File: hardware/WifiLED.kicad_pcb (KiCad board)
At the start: 2 copper layers, 63.5 x 45.7 mm, 22 parts, among them P1 CONN_01X03, P2 CONN_01X03, P3 CONN_01X01, P4 CONN_01X01, P5 CONN_01X01, P6 CONN_01X01

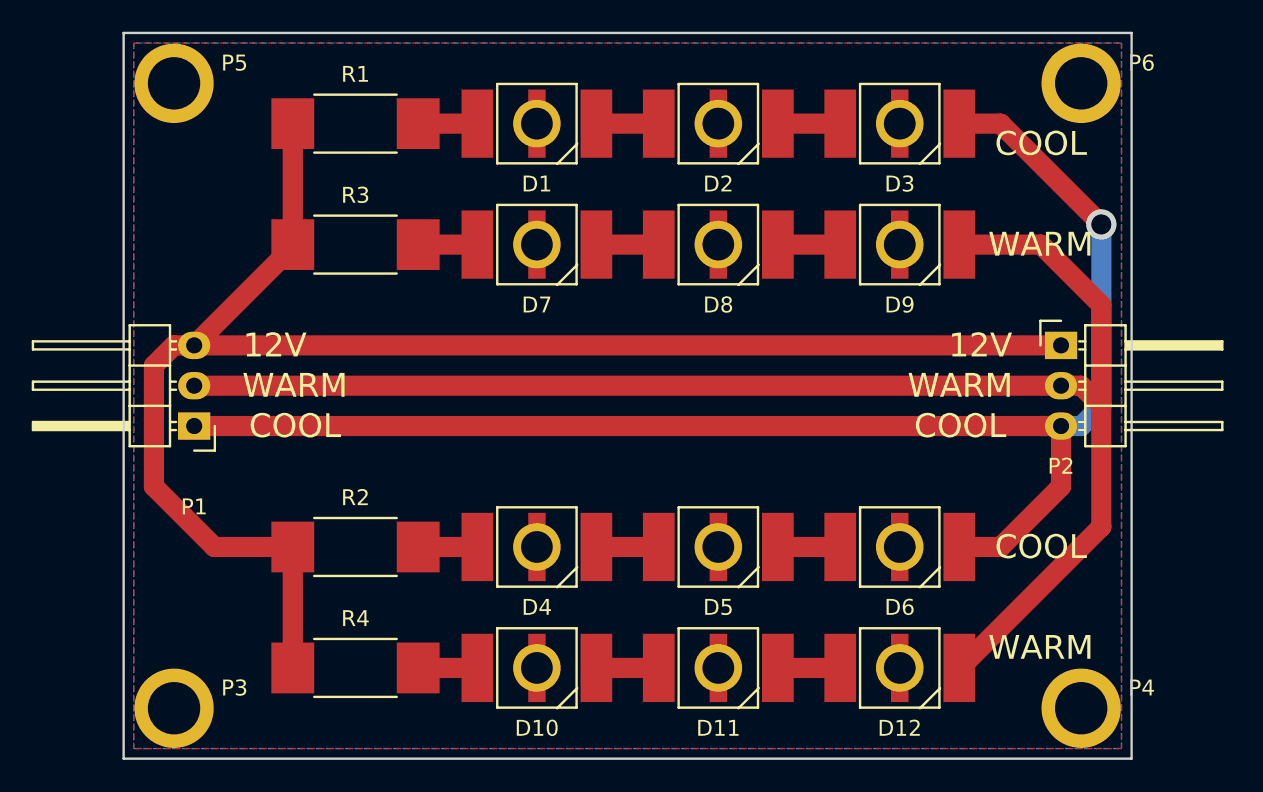
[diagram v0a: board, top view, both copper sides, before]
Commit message: Removed libopencm3 and software
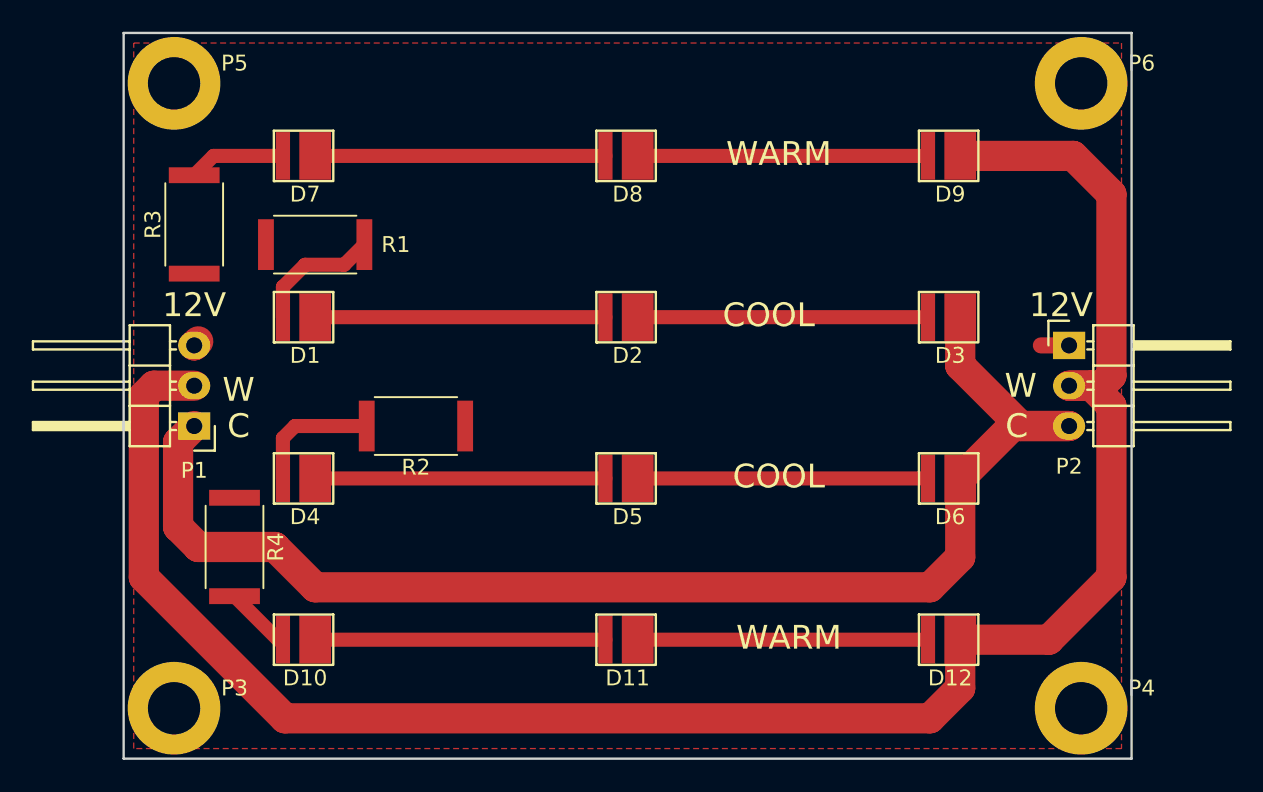
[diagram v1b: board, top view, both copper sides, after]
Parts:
- D1, D10, D11, D12, D2, D3, D4, D5, D6, D7, D8, D9: value LED_tm -> LED; footprint matthew:CREE_MX6 -> matthew:LED3030
- R1, R2, R3, R4: value 6.6R -> 8.2R; footprint Resistors_SMD:R_2512_HandSoldering -> Resistors_SMD:R_2512
- moved D1 18.9 mm to (143.5, 96.5), turned to 180 degrees
- moved D3 14.9 mm to (184.2, 96.5), turned to 180 degrees
- moved D2 14.5 mm to (163.8, 96.5), turned to 180 degrees
- moved D7 13.3 mm to (143.5, 86.4), turned to 180 degrees
- moved D4 13.0 mm to (143.5, 106.7), turned to 180 degrees
- moved D10 12.7 mm to (143.5, 116.8), turned to 180 degrees
- moved R4 10.8 mm to (137.2, 109.2), turned to 270 degrees
- moved R3 10.2 mm to (134.6, 88.9), turned to 90 degrees
- moved R2 8.52 mm to (148.6, 101.6), turned to 180 degrees
- moved R1 8.03 mm to (142.2, 90.2)
- moved D9 6.35 mm to (184.2, 86.4), turned to 180 degrees
- moved D6 5.68 mm to (184.2, 106.7), turned to 180 degrees
- moved D8 5.39 mm to (163.8, 86.4), turned to 180 degrees
- moved D12 5.08 mm to (184.2, 116.8), turned to 180 degrees
- moved D5 4.58 mm to (163.8, 106.7), turned to 180 degrees
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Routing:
- net +12V: track 99.8 -> 1.45 mm
- net Net-(D12-Pad1): track 94.8 -> 123.9 mm
- net Net-(D8-Pad1): track 3.93 -> 18.3 mm
- net Net-(D7-Pad1): track 3.93 -> 18.3 mm
- net Net-(D5-Pad1): track 3.93 -> 18.3 mm
- net Net-(D4-Pad1): track 3.93 -> 18.3 mm
- net Net-(D2-Pad1): track 3.93 -> 18.3 mm
- net Net-(D11-Pad1): track 3.93 -> 18.3 mm
- net Net-(D10-Pad1): track 3.93 -> 18.3 mm
- net Net-(D1-Pad1): track 3.93 -> 18.3 mm
- net Net-(D3-Pad1): track 95.0 -> 83.1 mm, vias 1 -> 0
- net Net-(D1-Pad2): track 3.73 -> 8.14 mm
- net Net-(D4-Pad2): track 3.73 -> 8.14 mm
- net Net-(D7-Pad2): track 3.73 -> 6.09 mm
- added copper zone on F.Cu, net +12V
- removed copper zone on B.Cu, net Net-(D1-Pad3)
- removed copper zone on F.Cu, net Net-(D1-Pad3)
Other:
- net class Fat: trace_width 1.27 -> 0.889
- board text added: "C"
- board text added: "W"
